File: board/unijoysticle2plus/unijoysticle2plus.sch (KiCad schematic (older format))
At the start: 34 parts, among them J1 DB9_Female, J2 DB9_Female, J3 Barrel_Jack, J4 Conn_01x03_Male, J5 USB_B_Micro, Q1 S8050, Q2 S8050, SW1 SW_Push, SW2 SW_SPST, SW3 SW_Push, SW4 SW_Push, U1 ESP32-WROOM-32D, U2 74LS05, U3 74LS05, U4 CH340C, U5 AP2114H-3_3TRG1

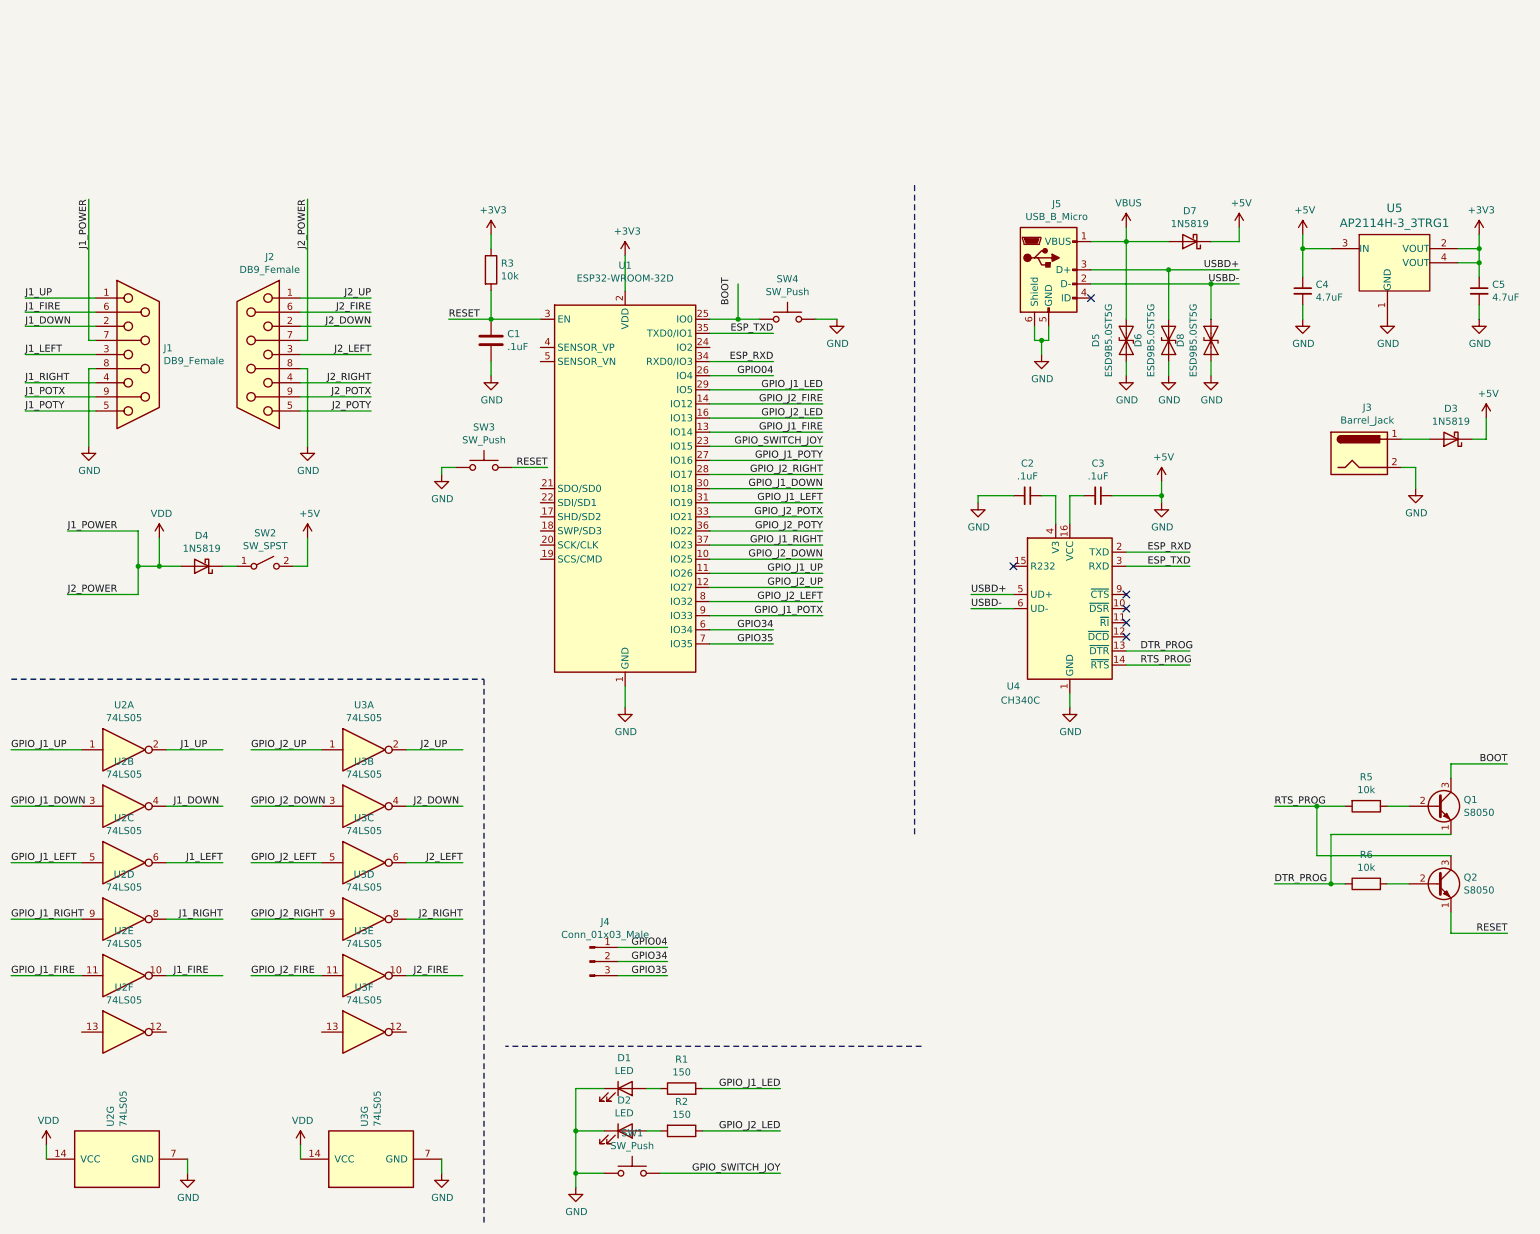
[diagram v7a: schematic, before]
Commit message: unijoysticle2plus: auto-reset circuit fixed and minor fixes
Transistor had B/E/C wrong.
Correct package for push buttons for reset & boot.
Improved package for 7405 (renamed it from 74lc05 to 74hc05).

Reset layout. Not working on it yet since schematic is not ready yet
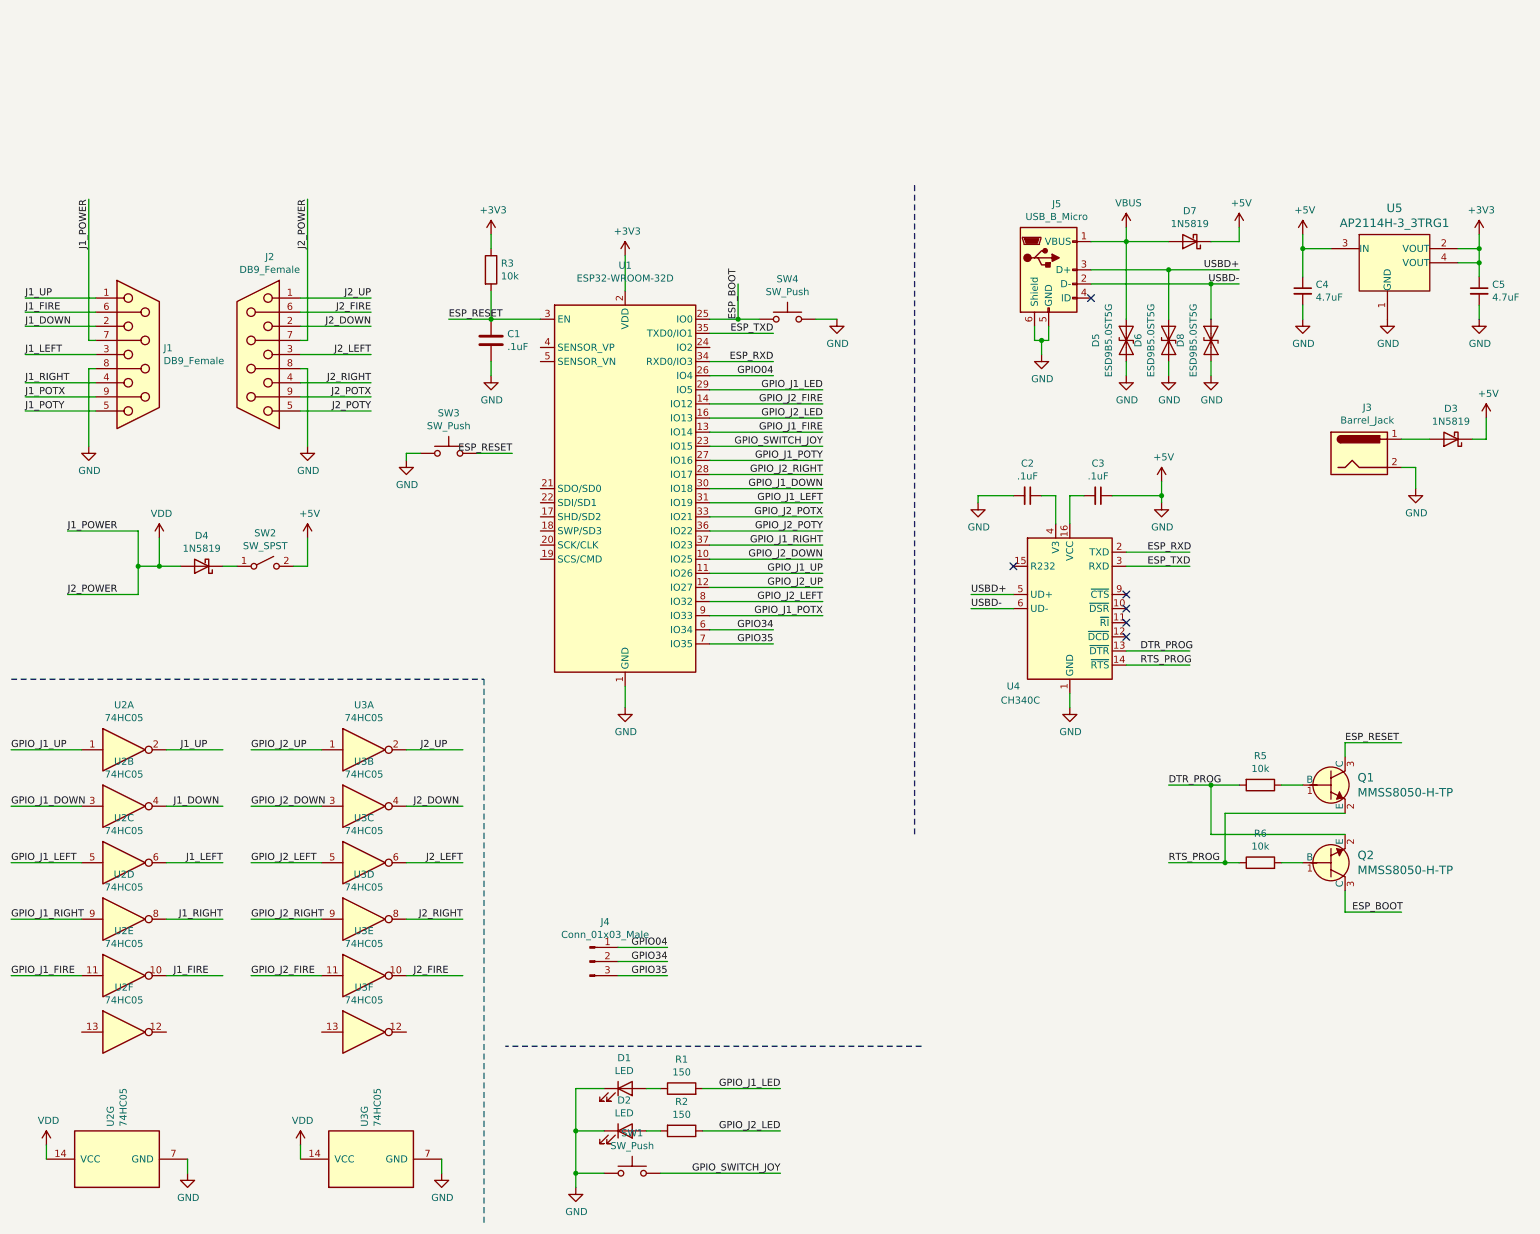
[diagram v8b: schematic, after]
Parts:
- removed Q1, Q2: S8050, Package_TO_SOT_THT:TO-92_Inline, symbol Transistor_BJT:S8050
- added Q1, Q2: MMSS8050-H-TP, Package_TO_SOT_SMD:SOT-23, symbol dk_Transistors-Bipolar-BJT-Single:MMSS8050-H-TP
- SW3, SW4: footprint Button_Switch_THT:SW_Tactile_Straight_KSA0Axx1LFTR -> Button_Switch_SMD:SW_SPST_B3U-1000P
- U2, U3: value 74LS05 -> 74HC05; footprint Silicon-Standard:SO14 -> Package_SO:SOIC-14_3.9x8.7mm_P1.27mm
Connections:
- net labels added: ESP_BOOT, ESP_RESET
- net labels removed: BOOT, RESET
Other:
- moved on the sheet: R5, R6, SW3
